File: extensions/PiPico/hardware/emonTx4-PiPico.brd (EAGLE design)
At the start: 48.8 x 53.3 mm, 8 parts, among them U1 RASPBERRY_PICOSMD

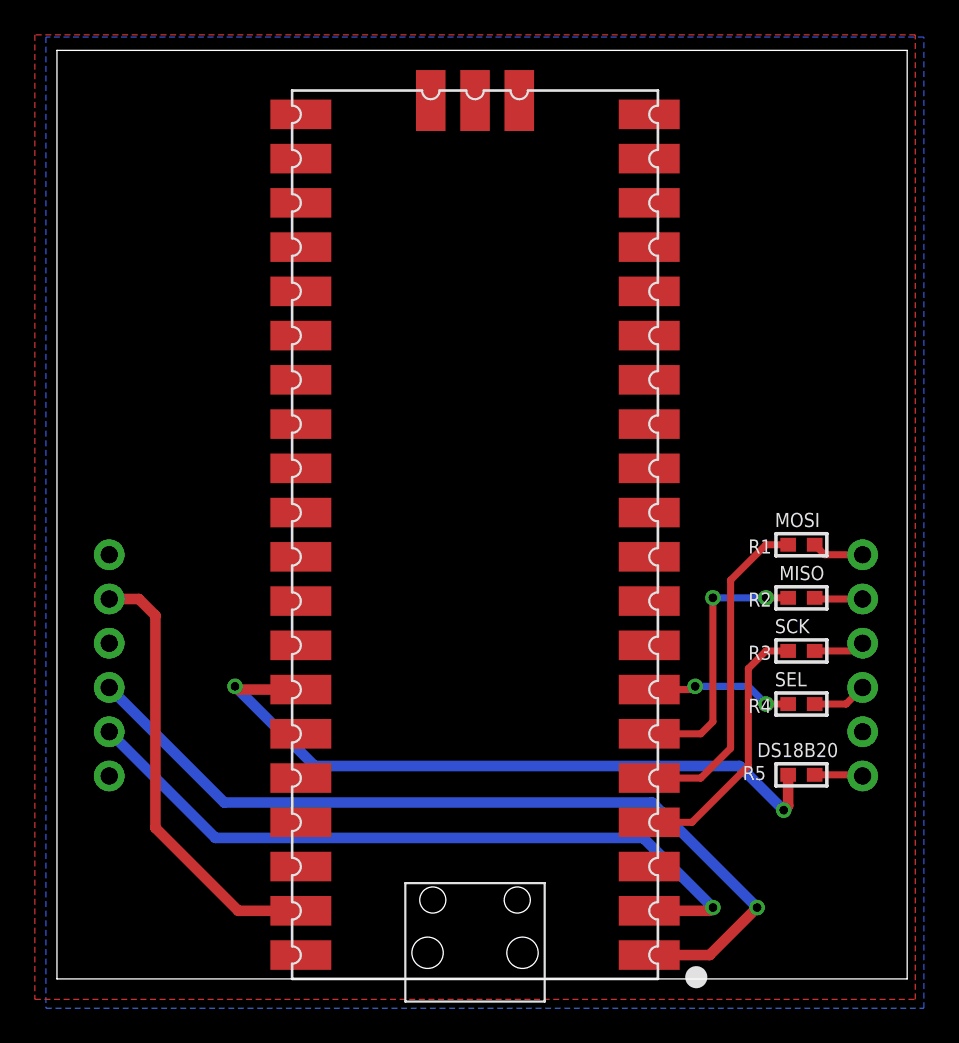
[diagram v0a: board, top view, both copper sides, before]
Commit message: updated pi pico extension design
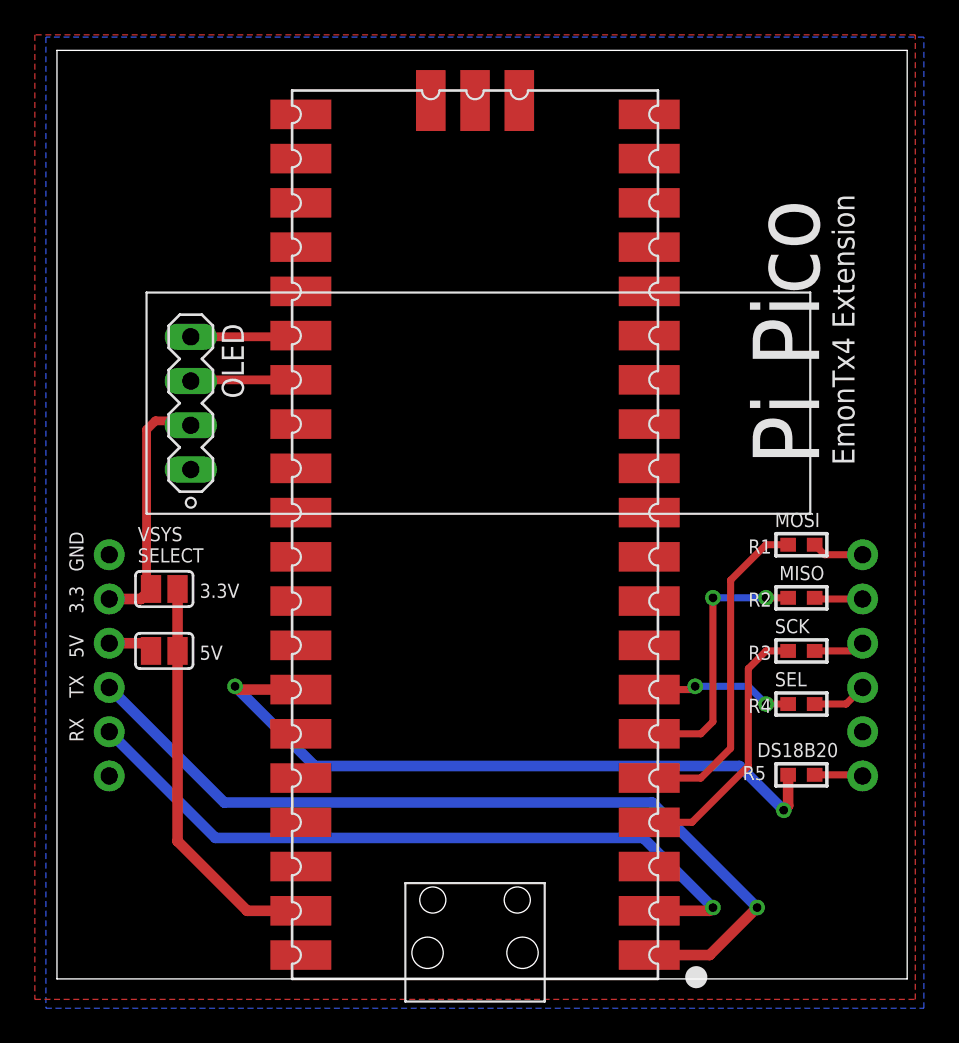
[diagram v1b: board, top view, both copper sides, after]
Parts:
- added OLED: (no value), con-lstb-db:MA04-1-OLED
- added SJ1, SJ2: (no value), jumper:SJ
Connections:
- new net 5V: JP1.4, SJ2.2
- new net N$1: SJ1.1, SJ2.1, U1.P$39
- new net SCL: OLED.2, U1.P$27
- new net SDA: OLED.1, U1.P$26
- net 3.3V: now also OLED.3, SJ1.2; no longer U1.P$39
- net GND: now also OLED.4
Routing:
- net N$1: track 0.00 -> 23.2 mm
- net 3.3V: track 25.6 -> 14.7 mm
- net SDA: track 0.00 -> 6.34 mm
- net SCL: track 0.00 -> 6.34 mm
- net 5V: track 0.00 -> 2.58 mm
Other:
- board text added: "3.3V"
- board text added: "5V"
- board text added: "EmonTx4 Extension"
- board text added: "Pi Pico"
- board text added: "VSYS SELECT"
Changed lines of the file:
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@@
 <board>
 <plain>
-<text x="5.016" y="25.383" size="0.8128" layer="26" font="vector" ratio="20" rot="MR90">GND</text>
-<text x="5.016" y="22.97" size="0.8128" layer="26" font="vector" ratio="20" rot="MR90">3.3</text>
-<text x="5.016" y="18.144" size="0.8128" layer="26" font="vector" ratio="20" rot="MR90">TX</text>
-<text x="5.016" y="15.604" size="0.8128" layer="26" font="vector" ratio="20" rot="MR90">RX</text>
+<text x="5.524" y="25.383" size="0.8128" layer="25" font="vector" ratio="20" rot="R90">GND</text>
+<text x="5.524" y="22.97" size="0.8128" layer="25" font="vector" ratio="20" rot="R90">3.3</text>
+<text x="5.524" y="18.144" size="0.8128" layer="25" font="vector" ratio="20" rot="R90">TX</text>
+<text x="5.524" y="15.604" size="0.8128" layer="25" font="vector" ratio="20" rot="R90">RX</text>
 <text x="45.212" y="27.94" size="0.8128" layer="25" font="vector" ratio="20">MOSI</text>
 <text x="45.466" y="24.892" size="0.8128" layer="25" font="vector" ratio="20">MISO</text>
@@
 <wire x1="4" y1="2" x2="52.808" y2="2" width="0" layer="20"/>
 <wire x1="4" y1="55.304" x2="4" y2="2" width="0" layer="20"/>
+<text x="5.524" y="20.43" size="0.8128" layer="25" font="vector" ratio="20" rot="R90">5V</text>
+<text x="8.636" y="25.908" size="0.8128" layer="25" font="vector" ratio="20">VSYS
+SELECT</text>
+<text x="12.192" y="23.876" size="0.8128" layer="25" font="vector" ratio="20">3.3V</text>
+<text x="12.192" y="20.32" size="0.8128" layer="25" font="vector" ratio="20">5V</text>
+<text x="47.752" y="31.496" size="3.81" layer="25" font="vector" ratio="20" rot="R90">Pi Pico</text>
+<text x="49.784" y="31.496" size="1.27" layer="25" font="vector" ratio="20" rot="R90">EmonTx4 Extension</text>
 </plain>
 <attributes>
@@
 </element>
 <element name="U1" library="RpiPico" package="PICO-PKG-SMD" value="RASPBERRY_PICOSMD" x="28" y="27.5" smashed="yes" rot="R180"/>
+<element name="SJ1" library="jumper" library_urn="urn:adsk.eagle:library:252" package="SJ" package3d_urn="urn:adsk.eagle:package:15471/1" value="" x="10.16" y="24.384" smashed="yes" rot="R180">
+<attribute name="POPULARITY" value="33" x="10.16" y="24.384" size="1.778" layer="27" rot="R180" display="off"/>
+<attribute name="VALUE" x="9.7599" y="24.384" size="0.02" layer="27" rot="R180"/>
+</element>
+<element name="SJ2" library="jumper" library_urn="urn:adsk.eagle:library:252" package="SJ" package3d_urn="urn:adsk.eagle:package:15471/1" value="" x="10.16" y="20.828" smashed="yes" rot="R180">
+<attribute name="POPULARITY" value="33" x="10.16" y="20.828" size="1.778" layer="27" rot="R180" display="off"/>
+<attribute name="VALUE" x="9.7599" y="20.828" size="0.02" layer="27" rot="R180"/>
+</element>
+<element name="OLED" library="con-lstb-db" package="MA04-1-OLED" value="" x="11.684" y="35.052" smashed="yes" rot="R270">
+<attribute name="NAME" x="13.462" y="39.624" size="1.27" layer="25" ratio="10" rot="R270"/>
+</element>
 </elements>
 <signals>
@@
 <contactref element="U1" pad="P$13"/>
 <contactref element="U1" pad="P$38"/>
+<contactref element="OLED" pad="4"/>
 </signal>
 <signal name="3.3V">
 <contactref element="JP1" pad="5"/>
-<contactref element="U1" pad="P$39"/>
-<wire x1="7" y1="23.81" x2="8.702" y2="23.81" width="0.6096" layer="1"/>
-<wire x1="8.702" y1="23.81" x2="9.652" y2="22.86" width="0.6096" layer="1"/>
-<wire x1="14.41" y1="5.91" x2="18" y2="5.91" width="0.6096" layer="1"/>
-<wire x1="9.652" y1="22.86" x2="9.652" y2="10.668" width="0.6096" layer="1"/>
-<wire x1="9.652" y1="10.668" x2="14.41" y2="5.91" width="0.6096" layer="1"/>
+<contactref element="SJ1" pad="2"/>
+<wire x1="9.398" y1="24.384" x2="8.824" y2="23.81" width="0.6096" layer="1"/>
+<wire x1="8.824" y1="23.81" x2="7" y2="23.81" width="0.6096" layer="1"/>
+<contactref element="OLED" pad="3"/>
+<wire x1="9.398" y1="24.384" x2="9.144" y2="24.638" width="0.508" layer="1"/>
+<wire x1="9.144" y1="33.528" x2="9.652" y2="34.036" width="0.508" layer="1"/>
+<wire x1="9.652" y1="34.036" x2="11.43" y2="34.036" width="0.508" layer="1"/>
+<wire x1="11.43" y1="34.036" x2="11.684" y2="33.782" width="0.508" layer="1"/>
+<wire x1="9.144" y1="24.638" x2="9.144" y2="33.528" width="0.508" layer="1"/>
 </signal>
 <signal name="DS18B20">
@@
 <wire x1="45.974" y1="11.938" x2="45.72" y2="11.684" width="0.6096" layer="1"/>
 </signal>
+<signal name="N$1">
+<contactref element="U1" pad="P$39"/>
+<contactref element="SJ1" pad="1"/>
+<contactref element="SJ2" pad="1"/>
+<wire x1="18" y1="5.91" x2="14.918" y2="5.91" width="0.6096" layer="1"/>
+<wire x1="10.922" y1="9.906" x2="10.922" y2="20.828" width="0.6096" layer="1"/>
+<wire x1="14.918" y1="5.91" x2="10.922" y2="9.906" width="0.6096" layer="1"/>
+<wire x1="10.922" y1="20.828" x2="10.922" y2="24.384" width="0.6096" layer="1"/>
+</signal>
+<signal name="5V">
+<contactref element="SJ2" pad="2"/>
+<contactref element="JP1" pad="4"/>
+<wire x1="9.398" y1="20.828" x2="8.956" y2="21.27" width="0.6096" layer="1"/>
+<wire x1="8.956" y1="21.27" x2="7" y2="21.27" width="0.6096" layer="1"/>
+</signal>
+<signal name="SDA">
+<contactref element="OLED" pad="1"/>
+<contactref element="U1" pad="P$26"/>
+<wire x1="18" y1="38.93" x2="17.932" y2="38.862" width="0.508" layer="1"/>
+<wire x1="17.932" y1="38.862" x2="11.684" y2="38.862" width="0.508" layer="1"/>
+</signal>
+<signal name="SCL">
+<contactref element="OLED" pad="2"/>
+<contactref element="U1" pad="P$27"/>
+<wire x1="18" y1="36.39" x2="11.752" y2="36.39" width="0.508" layer="1"/>
+<wire x1="11.752" y1="36.39" x2="11.684" y2="36.322" width="0.508" layer="1"/>
+</signal>
 </signals>
 <mfgpreviewcolors>
@@
 </board>
 </drawing>
+<compatibility>
+<note version="6.3" minversion="6.2.2" severity="warning">
+Since Version 6.2.2 text objects can contain more than one line,
+which will not be processed correctly with this version.
+</note>
+<note version="8.2" severity="warning">
+Since Version 8.2, EAGLE supports online libraries. The ids
+of those online libraries will not be understood (or retained)
+with this version.
+</note>
+<note version="8.3" severity="warning">
+Since Version 8.3, EAGLE supports URNs for individual library
+assets (packages, symbols, and devices). The URNs of those assets
+will not be understood (or retained) with this version.
+</note>
+<note version="8.3" severity="warning">
+Since Version 8.3, EAGLE supports the association of 3D packages
+with devices in libraries, schematics, and board files. Those 3D
+packages will not be understood (or retained) with this version.
+</note>
+</compatibility>
 </eagle>
